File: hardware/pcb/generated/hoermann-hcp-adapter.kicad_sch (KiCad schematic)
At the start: 5 parts, among them J1 HCP2 6P6C unshielded, AliExpr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, U1 ESP32-C3 Super Mini, U2 Isolated auto-direction RS485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

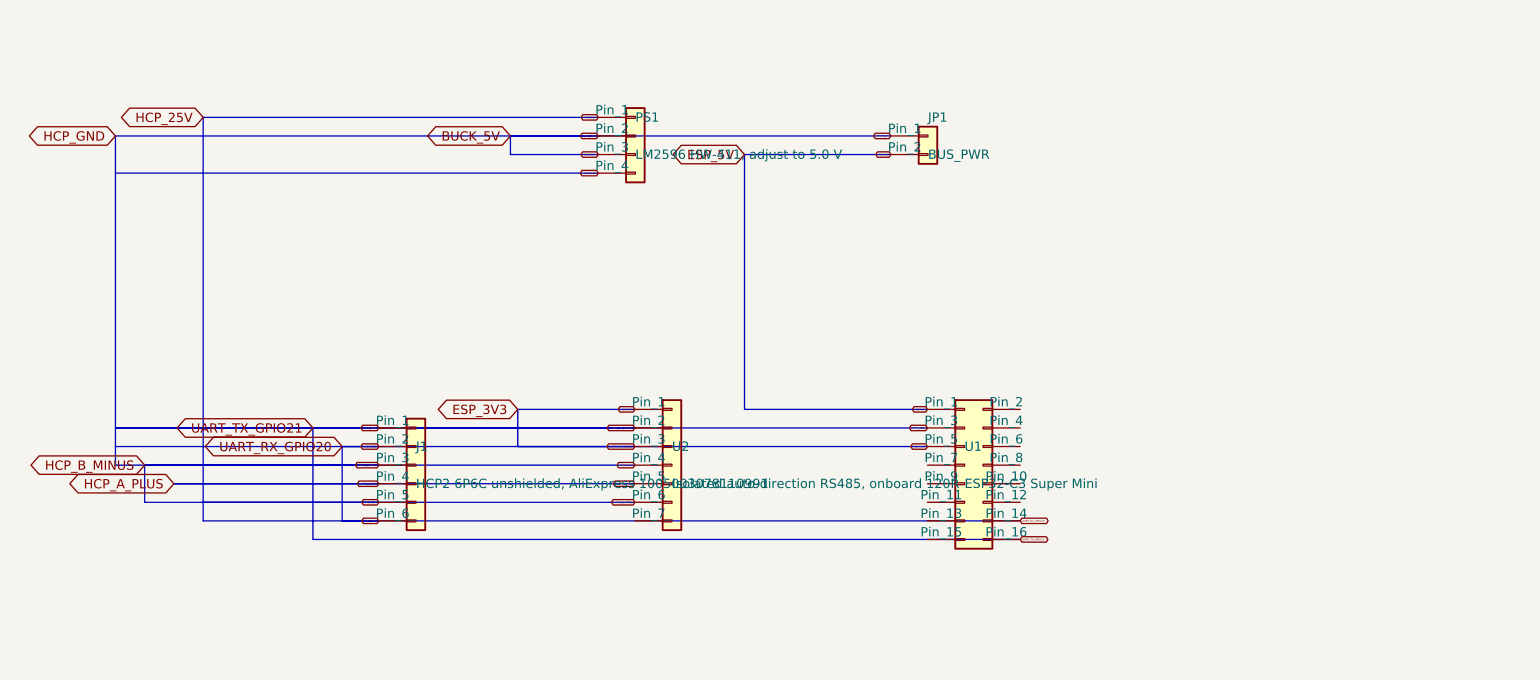
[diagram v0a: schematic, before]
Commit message: Generate the schematic directly as KiCad file, centre the PCB plot
schematic.py replaces the SKiDL flow: symbols with named pins, routed
wires, net labels and ground symbols are written straight to .kicad_sch,
then kicad-cli runs ERC, exports the netlist (checked against design.py)
and renders the PDF. SKiDL and the vendored symbol library are gone.
The PCB now sits centred on the A4 sheet of the layer PDF.

Co-Authored-By: Claude Fable 5.1 <noreply@anthropic.com>
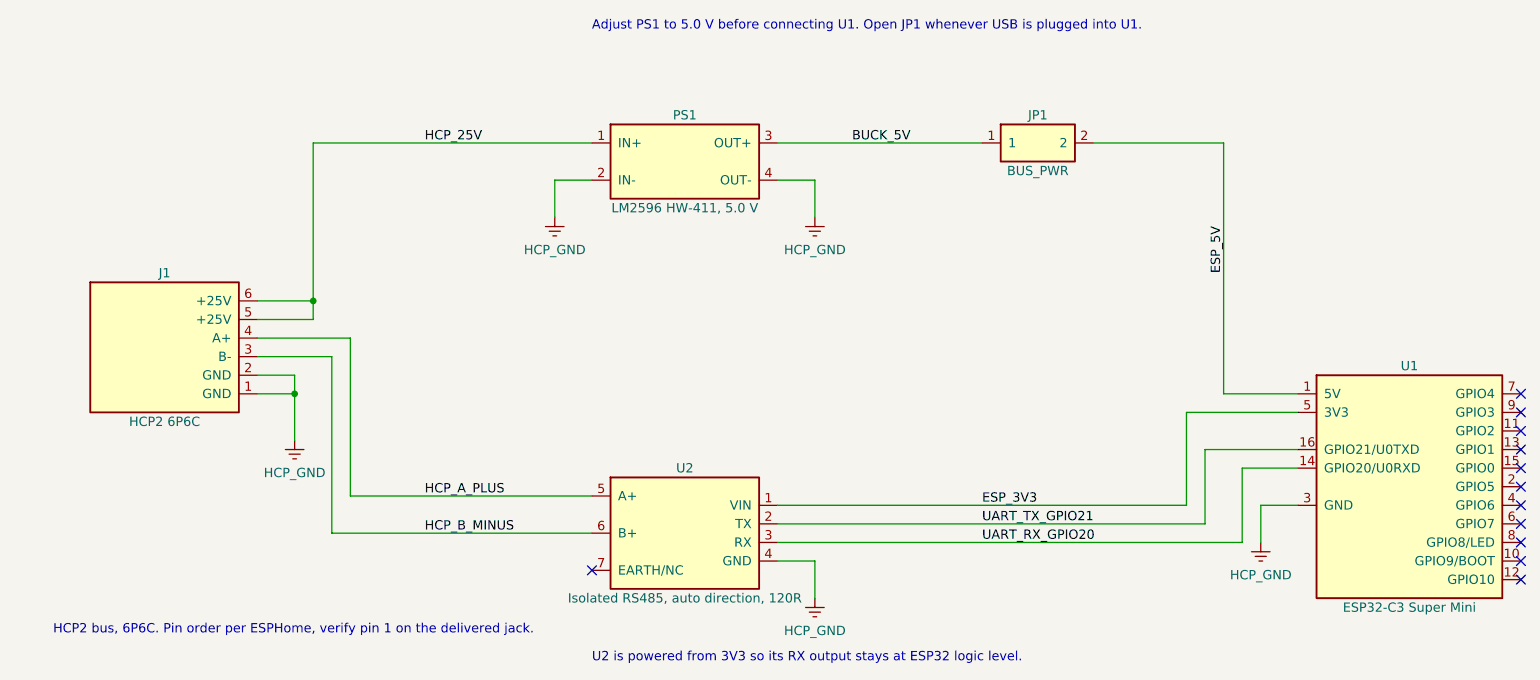
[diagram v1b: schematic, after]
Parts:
- removed J1: HCP2 6P6C unshielded, AliExpress 1005003078110991, HCP:RJ12_Amphenol_54601-x06_Horizontal, symbol Conn_01x06:Conn_01x06
- removed JP1: BUS_PWR, HCP:PinHeader_1x02_P2.54mm_Vertical, symbol Conn_01x02:Conn_01x02
- removed PS1: LM2596 HW-411, adjust to 5.0 V, HCP:LM2596_HW-411, symbol Conn_01x04:Conn_01x04
- removed U1: ESP32-C3 Super Mini, HCP:ESP32-C3_SuperMini, symbol Conn_02x08_Odd_Even:Conn_02x08_Odd_Even
- removed U2: Isolated auto-direction RS485, onboard 120R, HCP:RS485_Isolated_34x18, symbol Conn_01x07:Conn_01x07
- added J1: HCP2 6P6C, HCP:RJ12_Amphenol_54601-x06_Horizontal, symbol HCP:J1
- added JP1: BUS_PWR, HCP:PinHeader_1x02_P2.54mm_Vertical, symbol HCP:JP1
- added PS1: LM2596 HW-411, 5.0 V, HCP:LM2596_HW-411, symbol HCP:PS1
- added U1: ESP32-C3 Super Mini, HCP:ESP32-C3_SuperMini, symbol HCP:U1
- added U2: Isolated RS485, auto direction, 120R, HCP:RS485_Isolated_34x18, symbol HCP:U2
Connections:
- net BUCK_5V: now also JP1.1, PS1.3 (OUT+)
- net ESP_3V3: now also U1.5 (3V3), U2.1 (VIN)
- net ESP_5V: now also JP1.2, U1.1 (5V)
- net HCP_25V: now also J1.5 (+25V), J1.6 (+25V), PS1.1 (IN+)
- net HCP_A_PLUS: now also J1.4 (A+), U2.5 (A+)
- net HCP_B_MINUS: now also J1.3 (B-), U2.6 (B+)
- net HCP_GND: now also J1.1 (GND), J1.2 (GND), PS1.2 (IN-), PS1.4 (OUT-), U1.3 (GND), U2.4 (GND)
- net UART_RX_GPIO20: now also U1.14 (GPIO20/U0RXD), U2.3 (RX)
- net UART_TX_GPIO21: now also U1.16 (GPIO21/U0TXD), U2.2 (TX)
- no-connect marks 0 -> 12
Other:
- note added: "Adjust PS1 to 5.0 V before connecting U1. Open JP1 whenever USB is plugged into U1."
- note added: "HCP2 bus, 6P6C. Pin order per ESPHome, verify pin 1 on the delivered jack."
- note added: "U2 is powered from 3V3 so its RX output stays at ESP32 logic level."
- company: (none) -> Thies Gerken

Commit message: Regenerate outputs
Co-Authored-By: Claude Fable 5.1 <noreply@anthropic.com>
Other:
- note added: "HCP2 bus, 6P6C. Contact numbering per ESPHome HCP documentation."
- note removed: "HCP2 bus, 6P6C. Pin order per ESPHome, verify pin 1 on the delivered jack."
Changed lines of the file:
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@@
 (kicad_sch (version 20231120) (generator "hoermann-schematic") (generator_version "1")
   (paper "A4")
-  (title_block (title "Hörmann HCP2 ESP32-C3 Adapter") (date "2026-09-05") (rev "0d17945") (company "Thies Gerken"))
+  (title_block (title "Hörmann HCP2 ESP32-C3 Adapter") (date "2026-09-05") (rev "1b34439") (company "Thies Gerken"))
   (symbol (lib_id "HCP:J1") (at 40.64 88.9 0) (unit 1) (exclude_from_sim no) (in_bom yes) (on_board yes) (dnp no)
     (property "Reference" "J1" (at 40.64 78.74 0) (effects (font (size 1.27 1.27))))
@@
   (no_connect (at 226.06 118.11))
   (no_connect (at 226.06 120.65))
-  (text "HCP2 bus, 6P6C. Pin order per ESPHome, verify pin 1 on the delivered jack." (exclude_from_sim no) (at 25.4 128.27 0) (effects (font (size 1.27 1.27)) (justify left bottom)))
+  (text "HCP2 bus, 6P6C. Contact numbering per ESPHome HCP documentation." (exclude_from_sim no) (at 25.4 128.27 0) (effects (font (size 1.27 1.27)) (justify left bottom)))
   (text "Adjust PS1 to 5.0 V before connecting U1. Open JP1 whenever USB is plugged into U1." (exclude_from_sim no) (at 99.06 45.72 0) (effects (font (size 1.27 1.27)) (justify left bottom)))
   (text "U2 is powered from 3V3 so its RX output stays at ESP32 logic level." (exclude_from_sim no) (at 99.06 132.08 0) (effects (font (size 1.27 1.27)) (justify left bottom)))

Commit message: Regenerate outputs
Co-Authored-By: Claude Fable 5.1 <noreply@anthropic.com>
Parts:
- J1: footprint HCP:RJ12_Amphenol_54601-x06_Horizontal -> HCP:RJ12_95001_6P6C
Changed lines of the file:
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@@
 (kicad_sch (version 20231120) (generator "hoermann-schematic") (generator_version "1")
   (paper "A4")
-  (title_block (title "Hörmann HCP2 ESP32-C3 Adapter") (date "2026-09-05") (rev "1b34439") (company "Thies Gerken"))
+  (title_block (title "Hörmann HCP2 ESP32-C3 Adapter") (date "2026-09-05") (rev "33cb4bf") (company "Thies Gerken"))
   (symbol (lib_id "HCP:J1") (at 40.64 88.9 0) (unit 1) (exclude_from_sim no) (in_bom yes) (on_board yes) (dnp no)
     (property "Reference" "J1" (at 40.64 78.74 0) (effects (font (size 1.27 1.27))))
     (property "Value" "HCP2 6P6C" (at 40.64 99.06 0) (effects (font (size 1.27 1.27))))
-    (property "Footprint" "HCP:RJ12_Amphenol_54601-x06_Horizontal" (at 40.64 88.9 0) (effects (font (size 1.27 1.27)) (hide yes)))
+    (property "Footprint" "HCP:RJ12_95001_6P6C" (at 40.64 88.9 0) (effects (font (size 1.27 1.27)) (hide yes)))
     (property "Datasheet" "" (at 40.64 88.9 0) (effects (font (size 1.27 1.27)) (hide yes)))
     (pin "6")
